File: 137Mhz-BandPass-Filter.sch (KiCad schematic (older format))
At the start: 13 parts

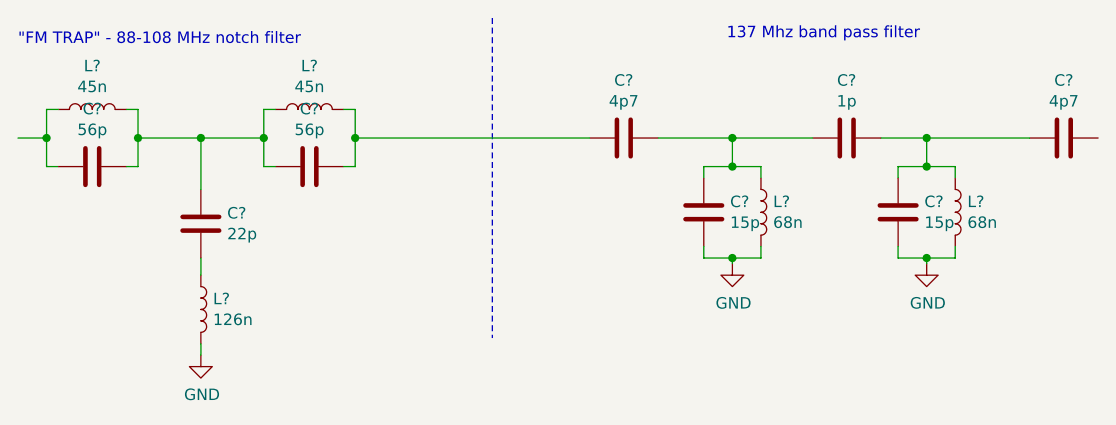
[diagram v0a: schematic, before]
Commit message: Footprints assigned
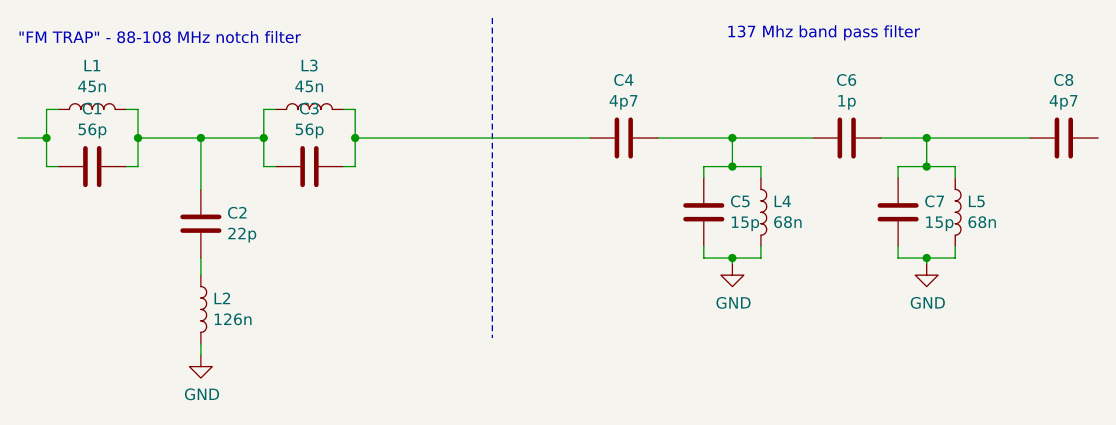
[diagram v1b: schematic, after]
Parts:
- C1, C2, C3, C4, C5, C6, C7, C8: renamed from C?; footprint (none) -> Capacitor_SMD:C_0603_1608Metric
- L1, L3: renamed from L?; footprint (none) -> Inductor_SMD:L_Neosid_Air-Coil_SML_2turn_HDM0231A
- L2: renamed from L?; footprint (none) -> Inductor_SMD:L_Neosid_Air-Coil_SML_5turn_HDM0531A
- L4, L5: renamed from L?; footprint (none) -> Inductor_SMD:L_Neosid_Air-Coil_SML_4turn_HDM0431A
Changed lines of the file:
@@
 EESchema Schematic File Version 4
+LIBS:137Mhz-BandPass-Filter-cache
 EELAYER 26 0
 EELAYER END
@@
 $EndDescr
 $Comp
-L device:C C?
+L device:C C4
 U 1 1 5C988072
 P 6125 3500
-F 0 "C?" V 5873 3500 50  0000 C CNN
+F 0 "C4" V 5873 3500 50  0000 C CNN
 F 1 "4p7" V 5964 3500 50  0000 C CNN
-F 2 "" H 6163 3350 50  0001 C CNN
+F 2 "Capacitor_SMD:C_0603_1608Metric" H 6163 3350 50  0001 C CNN
 F 3 "" H 6125 3500 50  0001 C CNN
 	1    6125 3500
@@
 $EndComp
 $Comp
-L device:L L?
+L device:L L4
 U 1 1 5C9880A3
 P 6725 3825
-F 0 "L?" H 6778 3871 50  0000 L CNN
+F 0 "L4" H 6778 3871 50  0000 L CNN
 F 1 "68n" H 6778 3780 50  0000 L CNN
-F 2 "" H 6725 3825 50  0001 C CNN
+F 2 "Inductor_SMD:L_Neosid_Air-Coil_SML_4turn_HDM0431A" H 6725 3825 50  0001 C CNN
 F 3 "" H 6725 3825 50  0001 C CNN
 	1    6725 3825
@@
 $EndComp
 $Comp
-L device:C C?
+L device:C C6
 U 1 1 5C988184
 P 7100 3500
-F 0 "C?" V 6848 3500 50  0000 C CNN
+F 0 "C6" V 6848 3500 50  0000 C CNN
 F 1 "1p" V 6939 3500 50  0000 C CNN
-F 2 "" H 7138 3350 50  0001 C CNN
+F 2 "Capacitor_SMD:C_0603_1608Metric" H 7138 3350 50  0001 C CNN
 F 3 "" H 7100 3500 50  0001 C CNN
 	1    7100 3500
@@
 $EndComp
 $Comp
-L device:C C?
+L device:C C8
 U 1 1 5C9881D4
 P 8050 3500
-F 0 "C?" V 7798 3500 50  0000 C CNN
+F 0 "C8" V 7798 3500 50  0000 C CNN
 F 1 "4p7" V 7889 3500 50  0000 C CNN
-F 2 "" H 8088 3350 50  0001 C CNN
+F 2 "Capacitor_SMD:C_0603_1608Metric" H 8088 3350 50  0001 C CNN
 F 3 "" H 8050 3500 50  0001 C CNN
 	1    8050 3500
@@
 $EndComp
 $Comp
-L device:C C?
+L device:C C5
 U 1 1 5C988200
 P 6475 3825
-F 0 "C?" H 6360 3779 50  0000 R CNN
+F 0 "C5" H 6360 3779 50  0000 R CNN
 F 1 "15p" H 6360 3870 50  0000 R CNN
-F 2 "" H 6513 3675 50  0001 C CNN
+F 2 "Capacitor_SMD:C_0603_1608Metric" H 6513 3675 50  0001 C CNN
 F 3 "" H 6475 3825 50  0001 C CNN
 	1    6475 3825
@@
 $EndComp
 $Comp
-L power:GND #PWR?
+L power:GND #PWR0101
 U 1 1 5C9883DD
 P 6600 4050
-F 0 "#PWR?" H 6600 3800 50  0001 C CNN
+F 0 "#PWR0101" H 6600 3800 50  0001 C CNN
 F 1 "GND" H 6605 3877 50  0000 C CNN
 F 2 "" H 6600 4050 50  0001 C CNN
@@
 Connection ~ 6600 3500
 $Comp
-L device:L L?
+L device:L L5
 U 1 1 5C988781
 P 7575 3825
-F 0 "L?" H 7628 3871 50  0000 L CNN
+F 0 "L5" H 7628 3871 50  0000 L CNN
 F 1 "68n" H 7628 3780 50  0000 L CNN
-F 2 "" H 7575 3825 50  0001 C CNN
+F 2 "Inductor_SMD:L_Neosid_Air-Coil_SML_4turn_HDM0431A" H 7575 3825 50  0001 C CNN
 F 3 "" H 7575 3825 50  0001 C CNN
 	1    7575 3825
@@
 $EndComp
 $Comp
-L device:C C?
+L device:C C7
 U 1 1 5C988787
 P 7325 3825
-F 0 "C?" H 7210 3779 50  0000 R CNN
+F 0 "C7" H 7210 3779 50  0000 R CNN
 F 1 "15p" H 7210 3870 50  0000 R CNN
-F 2 "" H 7363 3675 50  0001 C CNN
+F 2 "Capacitor_SMD:C_0603_1608Metric" H 7363 3675 50  0001 C CNN
 F 3 "" H 7325 3825 50  0001 C CNN
 	1    7325 3825
@@
 $EndComp
 $Comp
-L power:GND #PWR?
+L power:GND #PWR0102
 U 1 1 5C98878D
 P 7450 4050
-F 0 "#PWR?" H 7450 3800 50  0001 C CNN
+F 0 "#PWR0102" H 7450 3800 50  0001 C CNN
 F 1 "GND" H 7455 3877 50  0000 C CNN
 F 2 "" H 7450 4050 50  0001 C CNN
@@
 137 Mhz band pass filter
 $Comp
-L device:L L?
+L device:L L1
 U 1 1 5C988FFB
 P 3800 3375
-F 0 "L?" V 3990 3375 50  0000 C CNN
+F 0 "L1" V 3990 3375 50  0000 C CNN
 F 1 "45n" V 3899 3375 50  0000 C CNN
-F 2 "" H 3800 3375 50  0001 C CNN
+F 2 "Inductor_SMD:L_Neosid_Air-Coil_SML_2turn_HDM0231A" H 3800 3375 50  0001 C CNN
 F 3 "" H 3800 3375 50  0001 C CNN
 	1    3800 3375
@@
 $EndComp
 $Comp
-L device:C C?
+L device:C C1
 U 1 1 5C989001
 P 3800 3625
-F 0 "C?" V 3548 3625 50  0000 C CNN
+F 0 "C1" V 3548 3625 50  0000 C CNN
 F 1 "56p" V 3639 3625 50  0000 C CNN
-F 2 "" H 3838 3475 50  0001 C CNN
+F 2 "Capacitor_SMD:C_0603_1608Metric" H 3838 3475 50  0001 C CNN
 F 3 "" H 3800 3625 50  0001 C CNN
 	1    3800 3625
@@
 	3600 3500 3600 3375
 $Comp
-L device:C C?
+L device:C C2
 U 1 1 5C98A175
 P 4275 3875
-F 0 "C?" H 4160 3829 50  0000 R CNN
+F 0 "C2" H 4160 3829 50  0000 R CNN
 F 1 "22p" H 4160 3920 50  0000 R CNN
-F 2 "" H 4313 3725 50  0001 C CNN
+F 2 "Capacitor_SMD:C_0603_1608Metric" H 4313 3725 50  0001 C CNN
 F 3 "" H 4275 3875 50  0001 C CNN
 	1    4275 3875
@@
 $EndComp
 $Comp
-L device:L L?
+L device:L L2
 U 1 1 5C98A1C3
 P 4275 4250
-F 0 "L?" H 4328 4296 50  0000 L CNN
+F 0 "L2" H 4328 4296 50  0000 L CNN
 F 1 "126n" H 4328 4205 50  0000 L CNN
-F 2 "" H 4275 4250 50  0001 C CNN
+F 2 "Inductor_SMD:L_Neosid_Air-Coil_SML_5turn_HDM0531A" H 4275 4250 50  0001 C CNN
 F 3 "" H 4275 4250 50  0001 C CNN
 	1    4275 4250
@@
 $EndComp
 $Comp
-L power:GND #PWR?
+L power:GND #PWR0103
 U 1 1 5C98A221
 P 4275 4450
-F 0 "#PWR?" H 4275 4200 50  0001 C CNN
+F 0 "#PWR0103" H 4275 4200 50  0001 C CNN
 F 1 "GND" H 4280 4277 50  0000 C CNN
 F 2 "" H 4275 4450 50  0001 C CNN
@@
 $EndComp
 $Comp
-L device:L L?
+L device:L L3
 U 1 1 5C98A2C3
 P 4750 3375
-F 0 "L?" V 4940 3375 50  0000 C CNN
+F 0 "L3" V 4940 3375 50  0000 C CNN
 F 1 "45n" V 4849 3375 50  0000 C CNN
-F 2 "" H 4750 3375 50  0001 C CNN
+F 2 "Inductor_SMD:L_Neosid_Air-Coil_SML_2turn_HDM0231A" H 4750 3375 50  0001 C CNN
 F 3 "" H 4750 3375 50  0001 C CNN
 	1    4750 3375
@@
 $EndComp
 $Comp
-L device:C C?
+L device:C C3
 U 1 1 5C98A2C9
 P 4750 3625
-F 0 "C?" V 4498 3625 50  0000 C CNN
+F 0 "C3" V 4498 3625 50  0000 C CNN
 F 1 "56p" V 4589 3625 50  0000 C CNN
-F 2 "" H 4788 3475 50  0001 C CNN
+F 2 "Capacitor_SMD:C_0603_1608Metric" H 4788 3475 50  0001 C CNN
 F 3 "" H 4750 3625 50  0001 C CNN
 	1    4750 3625

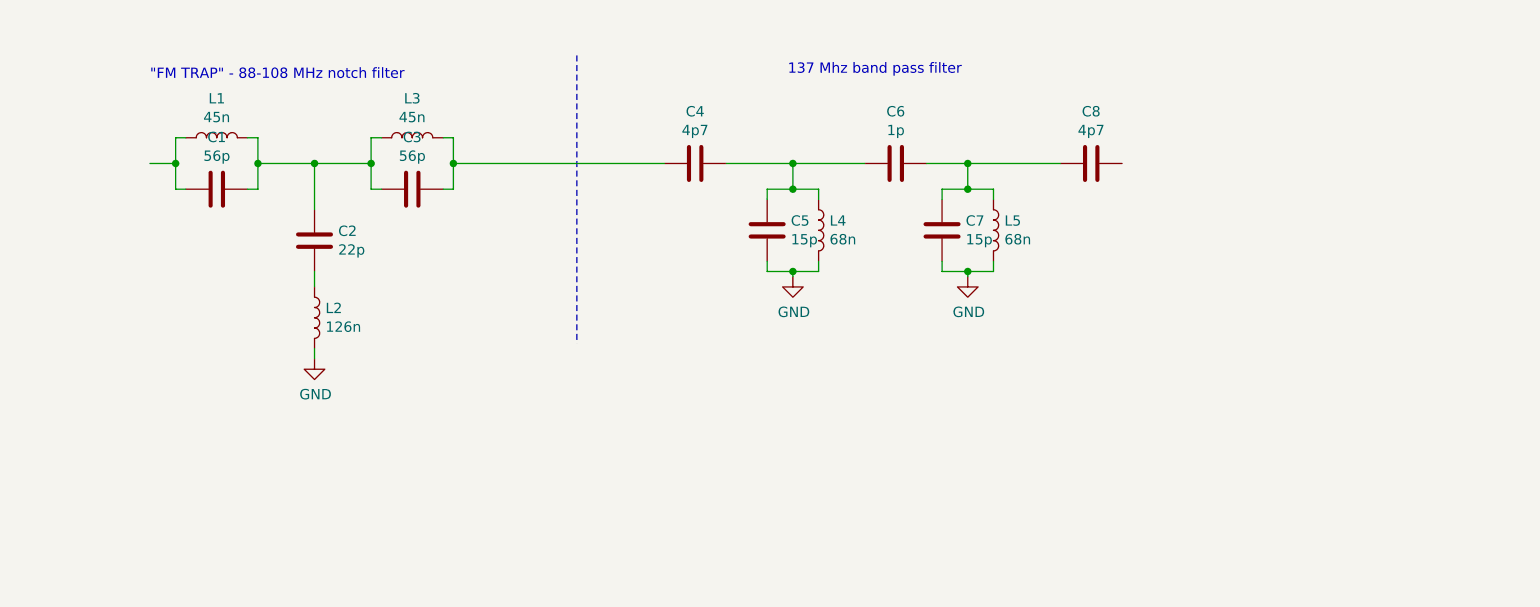
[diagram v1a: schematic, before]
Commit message: Added SMA connectors, first layout try
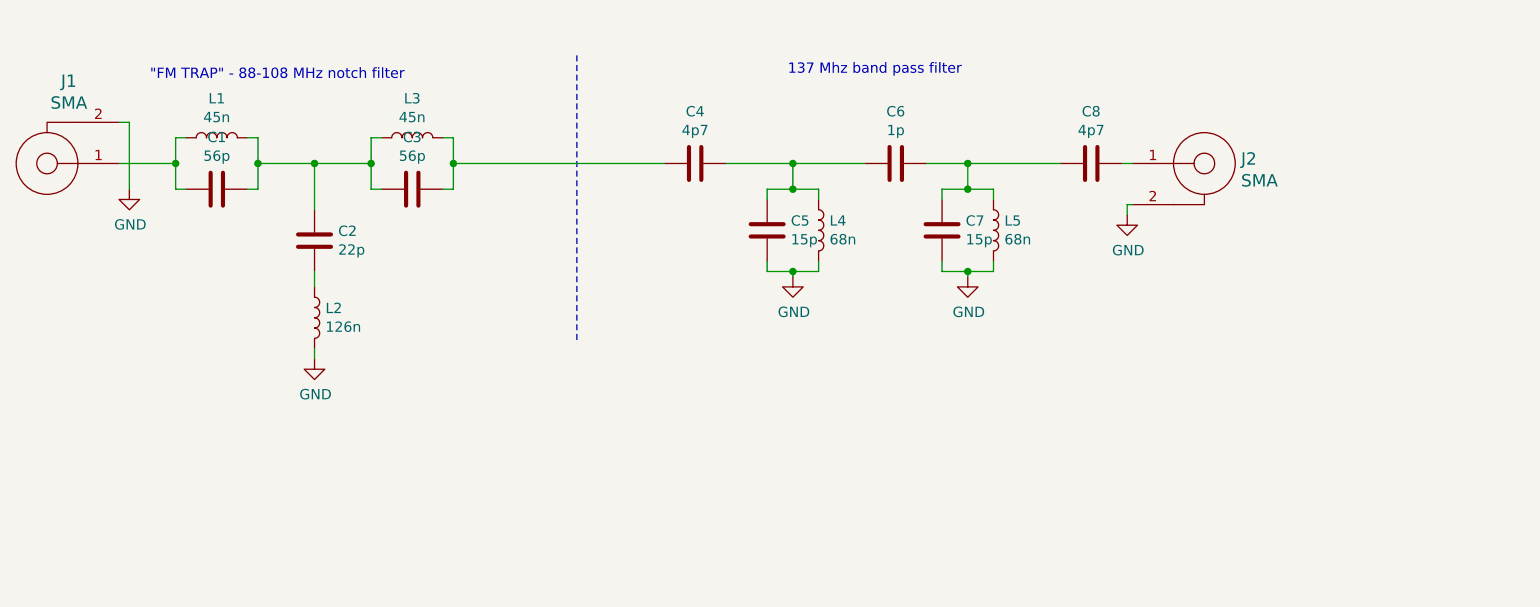
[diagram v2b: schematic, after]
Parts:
- added J1, J2: SMA, Connector_Coaxial:SMA_Molex_73251-1153_EdgeMount_Horizontal, symbol MLAB_CONNECTORS:SMA
- C1, C2, C3, C4, C5, C6, C7, C8: footprint Capacitor_SMD:C_0603_1608Metric -> Capacitor_SMD:C_0603_1608Metric_Pad0.99x1.00mm_HandSolder
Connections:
- net GND: now also J1.2, J2.2
- net at C8.1: now also J2.1
- net at C1.2, L1.1: now also J1.1
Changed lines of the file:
@@
 F 0 "C4" V 5873 3500 50  0000 C CNN
 F 1 "4p7" V 5964 3500 50  0000 C CNN
-F 2 "Capacitor_SMD:C_0603_1608Metric" H 6163 3350 50  0001 C CNN
+F 2 "Capacitor_SMD:C_0603_1608Metric_Pad0.99x1.00mm_HandSolder" H 6163 3350 50  0001 C CNN
 F 3 "" H 6125 3500 50  0001 C CNN
 	1    6125 3500
@@
 F 0 "C6" V 6848 3500 50  0000 C CNN
 F 1 "1p" V 6939 3500 50  0000 C CNN
-F 2 "Capacitor_SMD:C_0603_1608Metric" H 7138 3350 50  0001 C CNN
+F 2 "Capacitor_SMD:C_0603_1608Metric_Pad0.99x1.00mm_HandSolder" H 7138 3350 50  0001 C CNN
 F 3 "" H 7100 3500 50  0001 C CNN
 	1    7100 3500
@@
 F 0 "C8" V 7798 3500 50  0000 C CNN
 F 1 "4p7" V 7889 3500 50  0000 C CNN
-F 2 "Capacitor_SMD:C_0603_1608Metric" H 8088 3350 50  0001 C CNN
+F 2 "Capacitor_SMD:C_0603_1608Metric_Pad0.99x1.00mm_HandSolder" H 8088 3350 50  0001 C CNN
 F 3 "" H 8050 3500 50  0001 C CNN
 	1    8050 3500
@@
 F 0 "C5" H 6360 3779 50  0000 R CNN
 F 1 "15p" H 6360 3870 50  0000 R CNN
-F 2 "Capacitor_SMD:C_0603_1608Metric" H 6513 3675 50  0001 C CNN
+F 2 "Capacitor_SMD:C_0603_1608Metric_Pad0.99x1.00mm_HandSolder" H 6513 3675 50  0001 C CNN
 F 3 "" H 6475 3825 50  0001 C CNN
 	1    6475 3825
@@
 F 0 "C7" H 7210 3779 50  0000 R CNN
 F 1 "15p" H 7210 3870 50  0000 R CNN
-F 2 "Capacitor_SMD:C_0603_1608Metric" H 7363 3675 50  0001 C CNN
+F 2 "Capacitor_SMD:C_0603_1608Metric_Pad0.99x1.00mm_HandSolder" H 7363 3675 50  0001 C CNN
 F 3 "" H 7325 3825 50  0001 C CNN
 	1    7325 3825
@@
 F 0 "C1" V 3548 3625 50  0000 C CNN
 F 1 "56p" V 3639 3625 50  0000 C CNN
-F 2 "Capacitor_SMD:C_0603_1608Metric" H 3838 3475 50  0001 C CNN
+F 2 "Capacitor_SMD:C_0603_1608Metric_Pad0.99x1.00mm_HandSolder" H 3838 3475 50  0001 C CNN
 F 3 "" H 3800 3625 50  0001 C CNN
 	1    3800 3625
@@
 Wire Wire Line
 	3600 3375 3650 3375
-Wire Wire Line
-	3600 3500 3475 3500
 Connection ~ 3600 3500
 Wire Wire Line
@@
 F 0 "C2" H 4160 3829 50  0000 R CNN
 F 1 "22p" H 4160 3920 50  0000 R CNN
-F 2 "Capacitor_SMD:C_0603_1608Metric" H 4313 3725 50  0001 C CNN
+F 2 "Capacitor_SMD:C_0603_1608Metric_Pad0.99x1.00mm_HandSolder" H 4313 3725 50  0001 C CNN
 F 3 "" H 4275 3875 50  0001 C CNN
 	1    4275 3875
@@
 F 0 "C3" V 4498 3625 50  0000 C CNN
 F 1 "56p" V 4589 3625 50  0000 C CNN
-F 2 "Capacitor_SMD:C_0603_1608Metric" H 4788 3475 50  0001 C CNN
+F 2 "Capacitor_SMD:C_0603_1608Metric_Pad0.99x1.00mm_HandSolder" H 4788 3475 50  0001 C CNN
 F 3 "" H 4750 3625 50  0001 C CNN
 	1    4750 3625
@@
 Wire Notes Line
 	5550 2975 5550 4375
+$Comp
+L MLAB_CONNECTORS:SMA J1
+U 1 1 5C9A2C08
+P 2975 3500
+F 0 "J1" H 2869 3100 60  0000 C CNN
+F 1 "SMA" H 2869 3206 60  0000 C CNN
+F 2 "Connector_Coaxial:SMA_Molex_73251-1153_EdgeMount_Horizontal" H 2975 3500 60  0001 C CNN
+F 3 "" H 2975 3500 60  0000 C CNN
+	1    2975 3500
+	-1   0    0    1
+$EndComp
+$Comp
+L MLAB_CONNECTORS:SMA J2
+U 1 1 5C9A2DC6
+P 8600 3500
+F 0 "J2" H 8778 3522 60  0000 L CNN
+F 1 "SMA" H 8778 3416 60  0000 L CNN
+F 2 "Connector_Coaxial:SMA_Molex_73251-1153_EdgeMount_Horizontal" H 8600 3500 60  0001 C CNN
+F 3 "" H 8600 3500 60  0000 C CNN
+	1    8600 3500
+	1    0    0    -1
+$EndComp
+Wire Wire Line
+	8200 3500 8250 3500
+$Comp
+L power:GND #PWR0104
+U 1 1 5C9A39B3
+P 8225 3750
+F 0 "#PWR0104" H 8225 3500 50  0001 C CNN
+F 1 "GND" H 8230 3577 50  0000 C CNN
+F 2 "" H 8225 3750 50  0001 C CNN
+F 3 "" H 8225 3750 50  0001 C CNN
+	1    8225 3750
+	1    0    0    -1
+$EndComp
+Wire Wire Line
+	8250 3700 8225 3700
+Wire Wire Line
+	8225 3700 8225 3750
+Wire Wire Line
+	3325 3500 3600 3500
+$Comp
+L power:GND #PWR0105
+U 1 1 5C9A5252
+P 3375 3625
+F 0 "#PWR0105" H 3375 3375 50  0001 C CNN
+F 1 "GND" H 3380 3452 50  0000 C CNN
+F 2 "" H 3375 3625 50  0001 C CNN
+F 3 "" H 3375 3625 50  0001 C CNN
+	1    3375 3625
+	1    0    0    -1
+$EndComp
+Wire Wire Line
+	3325 3300 3375 3300
+Wire Wire Line
+	3375 3300 3375 3625
 $EndSCHEMATC

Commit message: Added 1515SQ-68N coils
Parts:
- L4, L5: footprint Inductor_SMD:L_Neosid_Air-Coil_SML_4turn_HDM0431A -> kicad-footprints-master:1515SQ-68N
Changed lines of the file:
@@
 F 0 "L4" H 6778 3871 50  0000 L CNN
 F 1 "68n" H 6778 3780 50  0000 L CNN
-F 2 "Inductor_SMD:L_Neosid_Air-Coil_SML_4turn_HDM0431A" H 6725 3825 50  0001 C CNN
+F 2 "kicad-footprints-master:1515SQ-68N" H 6725 3825 50  0001 C CNN
 F 3 "" H 6725 3825 50  0001 C CNN
 	1    6725 3825
@@
 F 0 "L5" H 7628 3871 50  0000 L CNN
 F 1 "68n" H 7628 3780 50  0000 L CNN
-F 2 "Inductor_SMD:L_Neosid_Air-Coil_SML_4turn_HDM0431A" H 7575 3825 50  0001 C CNN
+F 2 "kicad-footprints-master:1515SQ-68N" H 7575 3825 50  0001 C CNN
 F 3 "" H 7575 3825 50  0001 C CNN
 	1    7575 3825
